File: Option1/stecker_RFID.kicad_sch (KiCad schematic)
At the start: 1 part, among them J1301 Conn_01x02_Socket

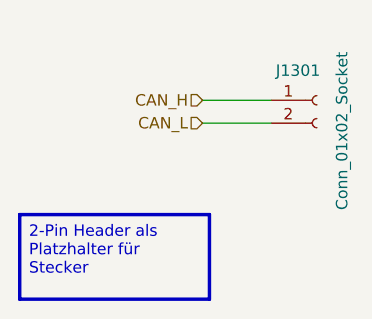
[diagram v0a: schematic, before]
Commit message: SPI Flash hinzugefügt, IN/Outputs vereinheitlicht, USB Flash Möglichkeit hinzugefügt, Display fehtl noch
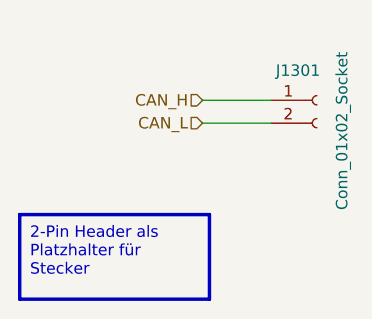
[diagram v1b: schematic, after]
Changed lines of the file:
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@@
 (kicad_sch
-	(version 20231120)
+	(version 20250114)
 	(generator "eeschema")
-	(generator_version "8.0")
+	(generator_version "9.0")
 	(paper "A4")
 	(title_block
@@
 		(comment 2 "Bachelorarbiet")
 		(comment 3 "Sebastian Hampl")
+	)
+	(text_box "2-Pin Header als Platzhalter für Stecker"
+		(exclude_from_sim no)
+		(at 20.32 39.37 0)
+		(size 21.082 9.398)
+		(margins 1.143 1.143 1.143 1.143)
+		(stroke
+			(width 0.381)
+			(type default)
+			(color 251 0 0 1)
+		)
+		(fill
+			(type none)
+		)
+		(effects
+			(font
+				(size 1.27 1.27)
+				(color 255 0 0 1)
+			)
+			(justify left top)
+		)
 	)
 	(wire
@@
 		)
 	)
-	(text_box "2-Pin Header als Platzhalter für Stecker"
-		(exclude_from_sim no)
-		(at 20.32 39.37 0)
-		(size 21.082 9.398)
-		(stroke
-			(width 0.381)
-			(type default)
-			(color 251 0 0 1)
-		)
-		(fill
-			(type none)
-		)
-		(effects
-			(font
-				(size 1.27 1.27)
-				(color 255 0 0 1)
-			)
-			(justify left top)
-		)
-	)
